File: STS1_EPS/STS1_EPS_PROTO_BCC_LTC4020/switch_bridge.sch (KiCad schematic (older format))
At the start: 8 parts, among them U2 SI7272DP-T1-GE3, U3 SI7272DP-T1-GE3

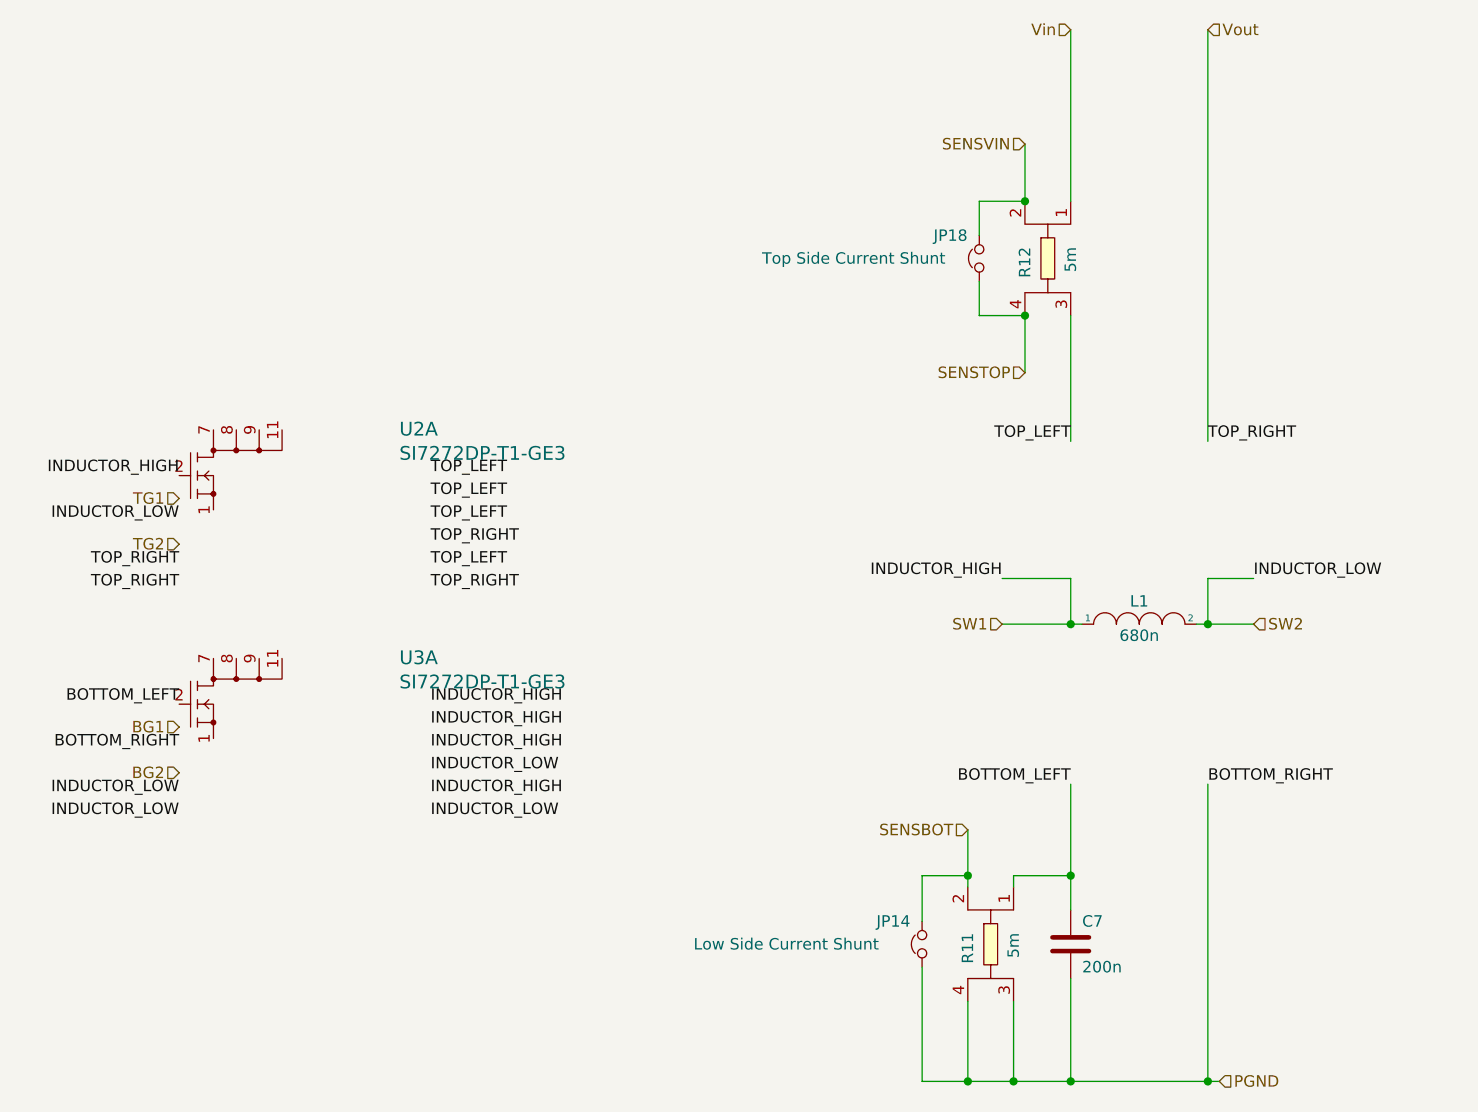
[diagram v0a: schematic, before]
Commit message: Incorporated feedback into BCC and SCC - Fixed "unspecified" pin type warnings - Added correct test point symbols - Added thermal blockers - Added DRC parameters and fixed DRC issues - Adapted CubeSat STS1 PCB template to not violate DRC
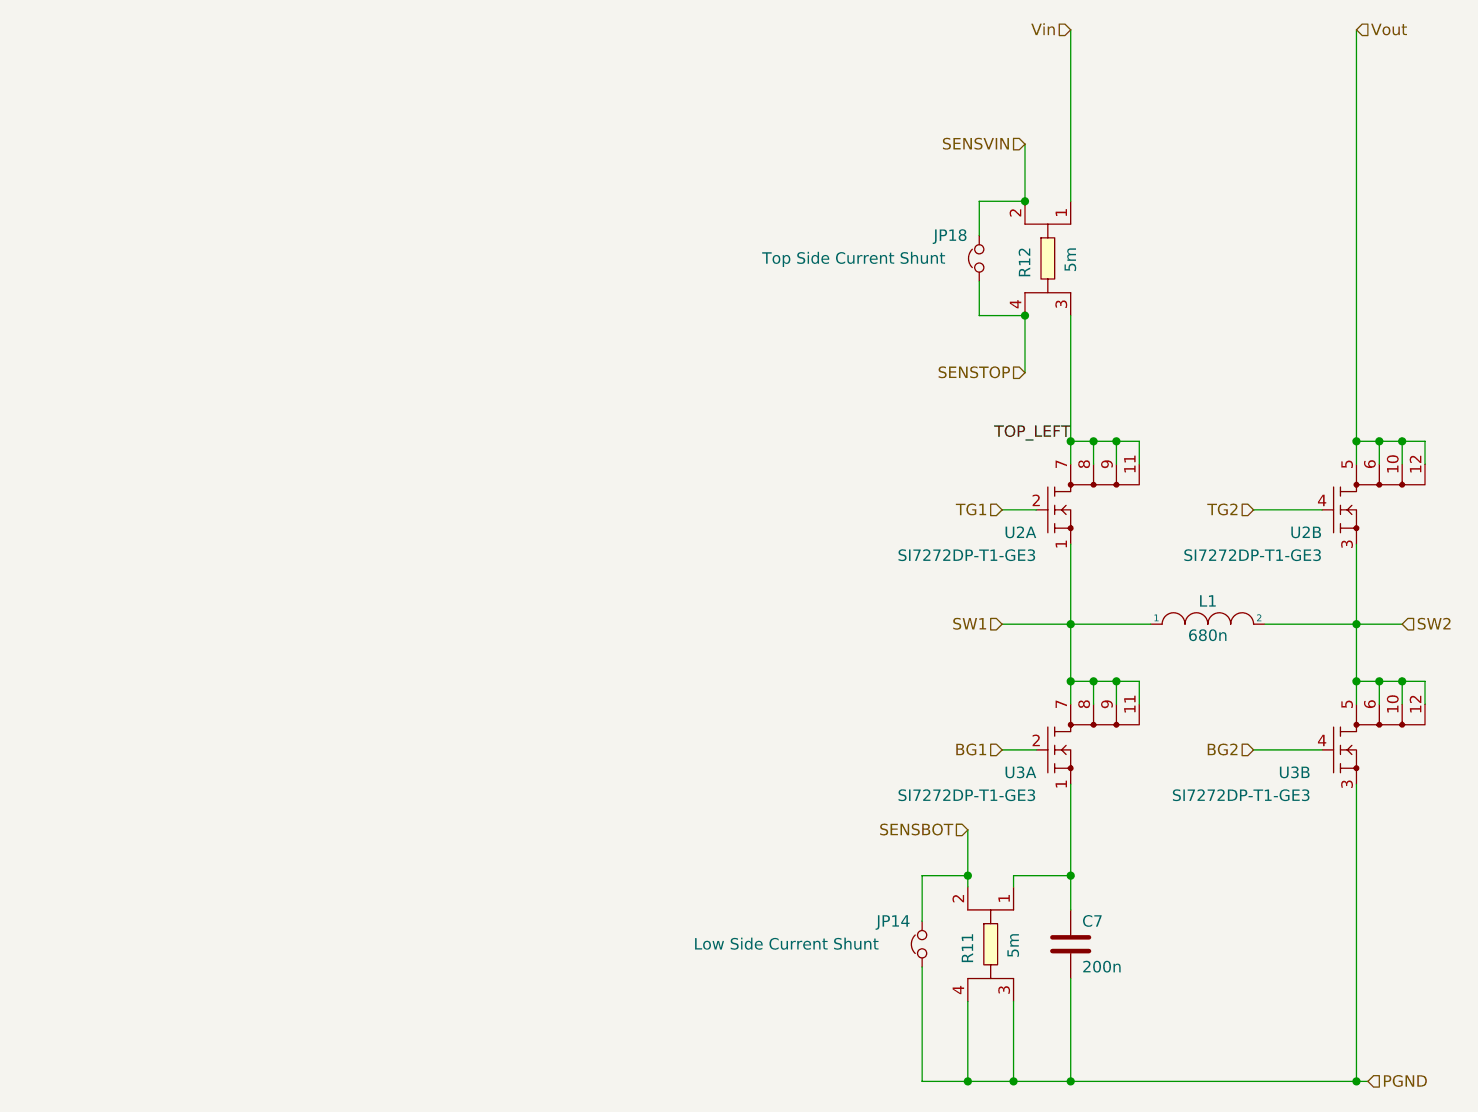
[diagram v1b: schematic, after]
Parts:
- added unit 2 of U2
- added unit 2 of U3
- U2, U3: footprint footprints:SI7288DPT1GE3 -> SI7288DPT1GE3; Manufacturer_Name (none) -> Vishay
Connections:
- net BG1: now also U3.2 (G1)
- net BG2: now also U3.4 (G2)
- net PGND: now also U3.3 (S2)
- net SW1: now also U2.1 (S1), U3.11 (D1_4), U3.7 (D1_1), U3.8 (D1_2), U3.9 (D1_3); no longer U2.2 (G1)
- net SW2: now also U2.3 (S2), U3.10 (D2_3), U3.12 (D2_4), U3.5 (D2_1), U3.6 (D2_2)
- net TG1: now also U2.2 (G1)
- net TG2: now also U2.4 (G2)
- net TOP_LEFT: now also U2.11 (D1_4), U2.7 (D1_1), U2.8 (D1_2), U2.9 (D1_3)
- net Vout: now also U2.10 (D2_3), U2.12 (D2_4), U2.5 (D2_1), U2.6 (D2_2)
- net at U3.1 (S1): now also C7.2, R11.1
- removed net BOTTOM_LEFT: C7.2, R11.1, U3.2 (G1)
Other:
- moved on the sheet: L1
